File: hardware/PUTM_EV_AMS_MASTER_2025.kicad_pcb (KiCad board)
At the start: 4 copper layers, 60 x 100 mm, 161 parts, among them IC1 3.3V/0.5A, IC11 ISO6760, IC2 TPS54202HDDCR, IC4 ADS131M04, IC5 LTC1799, IC6 LTC6820IMS, IC7 ISO6760, IC8 3.3V/0.5A, J1 M80-5100642, J10 M300-MV10345M1, J12 M80-51034XX, J2 USB_C_Receptacle_USB2.0_14P, J3 M80-51014XX, J4 FTSH-107-01-L-D-K, J5 M80-51004XX, J7 M300-MV10345M1, J8 M80-51004XX, K1 IMB03ITS, U1 MCP2542FD-E/MF, U10 STM32G484VEHx, U12 LMR33640DDDA, U2 LM397, U3 74AUP1G32, U4 UCC12040DVE, U6 MCP2542FD-E/MF, U7 MCP2542FD-E/MF, Y1 X322516MLB4SI

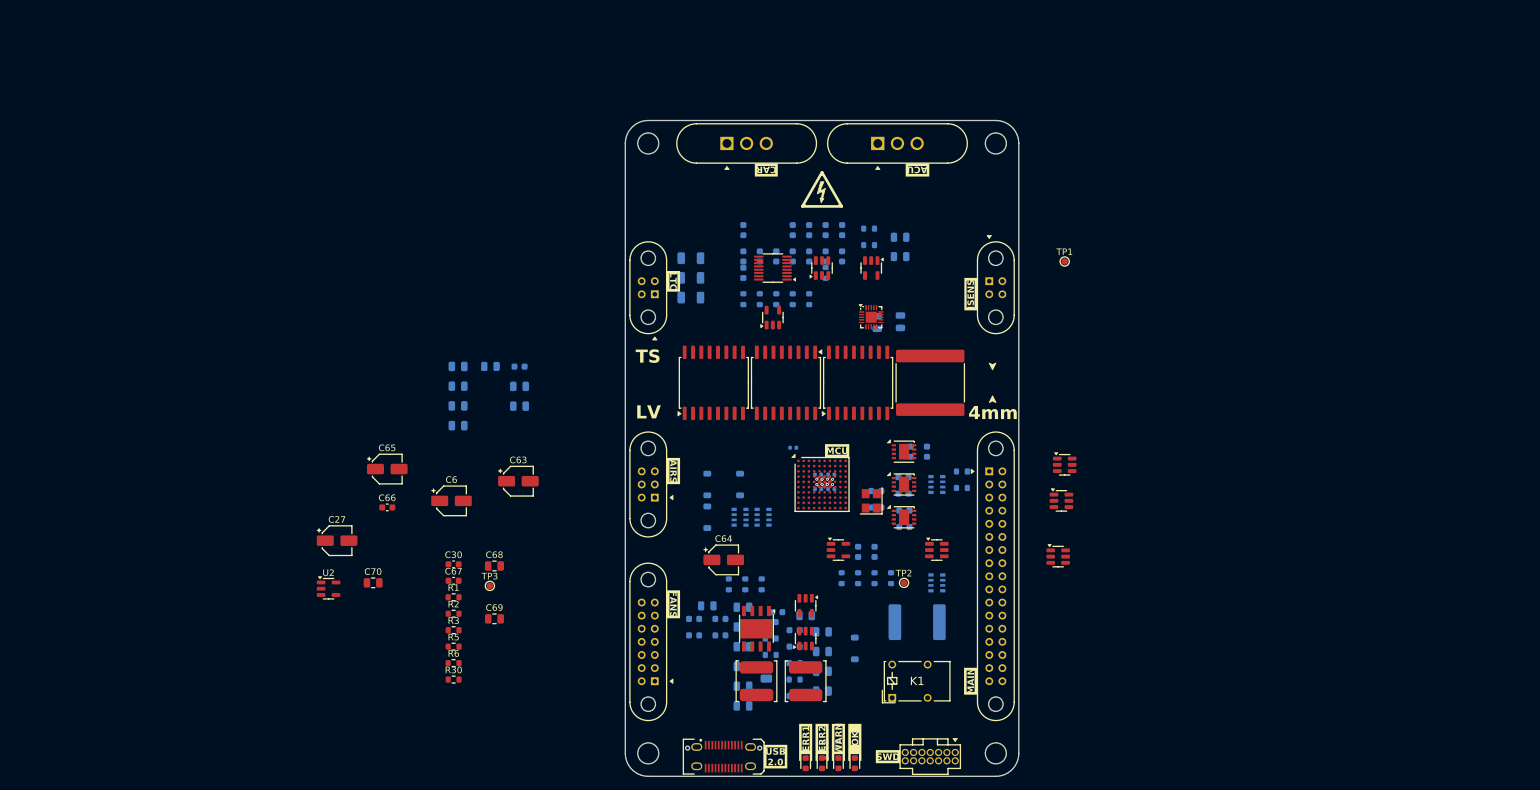
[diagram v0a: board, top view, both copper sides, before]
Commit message: all but the communications sections done
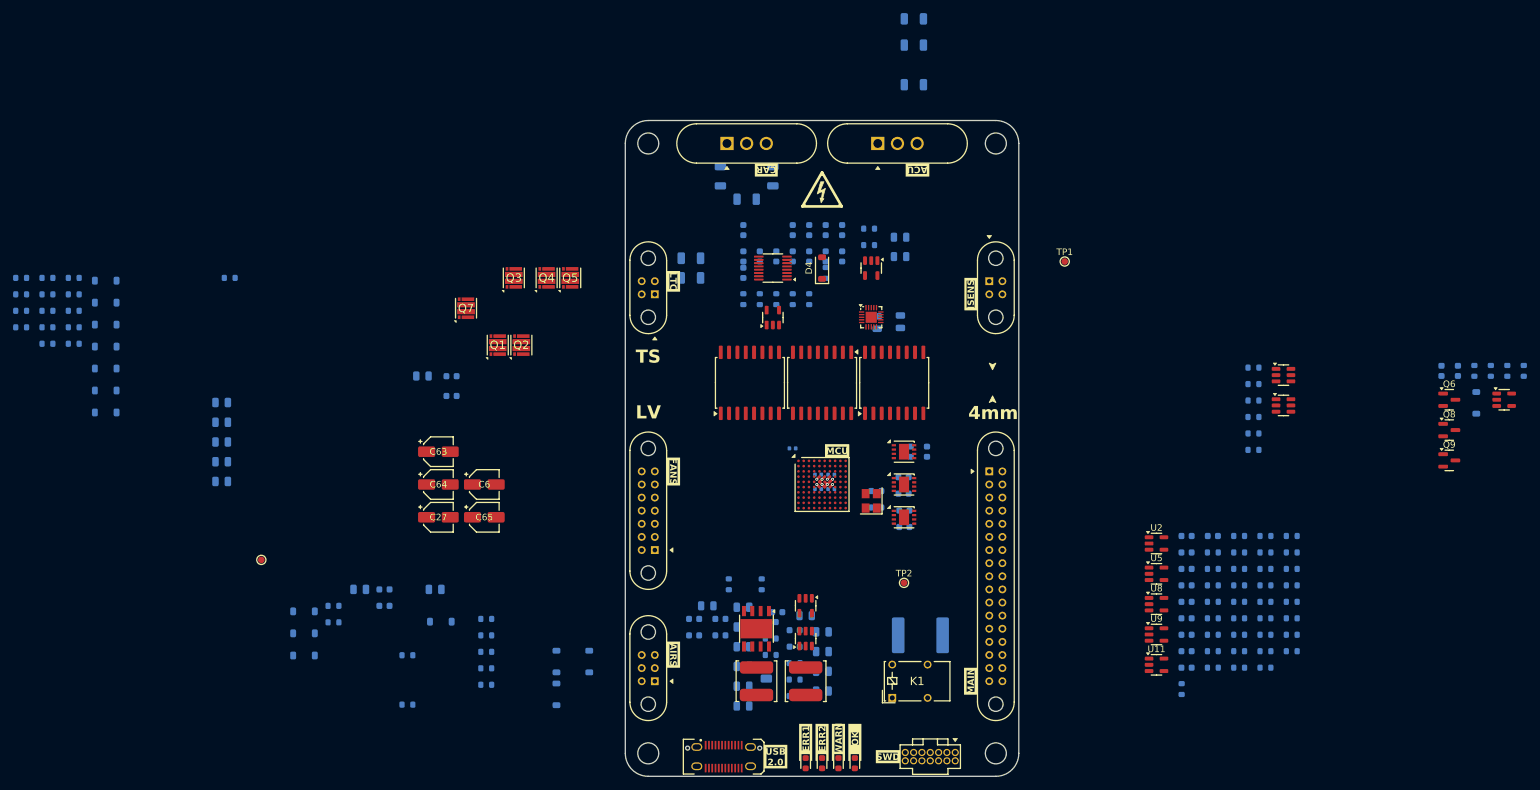
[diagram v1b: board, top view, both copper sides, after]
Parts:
- removed C53: 5.6nF/2000V, Capacitor_SMD:C_3640_9110Metric
- removed D13: ESDA25SC6Y, Package_TO_SOT_SMD:SOT-23-6
- removed RN11: 100, Resistor_SMD:R_Array_Convex_4x0603
- removed RN12: 10k, Resistor_SMD:R_Array_Convex_4x0603
- removed RN16: 1k, Resistor_SMD:R_Array_Convex_4x0603
- removed RN17: 4x100, Resistor_SMD:R_Array_Convex_4x0603
- removed RN7: 4x1k, Resistor_SMD:R_Array_Convex_4x0603
- added C71: 100nF, Capacitor_SMD:C_0603_1608Metric, B.Cu at (300.6, 115.9)
- added C72: 10nF, Capacitor_SMD:C_0603_1608Metric, B.Cu at (300.6, 118.4)
- added C73: 100nF, Capacitor_SMD:C_0603_1608Metric, B.Cu at (300.6, 120.9)
- added C74: 10nF, Capacitor_SMD:C_0603_1608Metric, B.Cu at (300.6, 123.4)
- added C75: 100nF, Capacitor_SMD:C_0603_1608Metric, B.Cu at (300.6, 125.9)
- added C76: 10nF, Capacitor_SMD:C_0603_1608Metric, B.Cu at (300.6, 128.4)
- added C77: 100nF, Capacitor_SMD:C_0603_1608Metric, B.Cu at (304.6, 108.4)
- added D14: 6V, Diode_SMD:D_SOD-123, B.Cu at (166.0, 119.8)
- added D15: 0.5V/1A, Diode_SMD:D_SOD-123, B.Cu at (166.0, 126.6)
- added D16: 30V, Diode_SMD:D_SOD-123, B.Cu at (166.0, 123.2)
- added D17: VSSB410S-E3/52T, Diode_SMD:D_SOD-123, B.Cu at (135.8, 72.8)
- added D18: VSSB410S-E3/52T, Diode_SMD:D_SOD-123, B.Cu at (135.8, 76.1)
- added D19: VSSB410S-E3/52T, Diode_SMD:D_SOD-123, B.Cu at (135.8, 79.5)
- added D20: VSSB410S-E3/52T, Diode_SMD:D_SOD-123, B.Cu at (135.8, 82.8)
- added D21: VSSB410S-E3/52T, Diode_SMD:D_SOD-123, B.Cu at (135.8, 86.2)
- added D22: VSSB410S-E3/52T, Diode_SMD:D_SOD-123, B.Cu at (135.8, 89.5)
- added D8: VSSB410S-E3/52T, Diode_SMD:D_SOD-123, B.Cu at (135.8, 69.4)
- added Q1: DMT6018LDR-7, Samacsys:DMT6018LDR7, F.Cu at (195.6, 79.2)
- added Q2: DMT6018LDR-7, Samacsys:DMT6018LDR7, F.Cu at (199.2, 79.2)
- added Q3: DMT6018LDR-7, Samacsys:DMT6018LDR7, F.Cu at (198.0, 69.0)
- added Q4: DMT6018LDR-7, Samacsys:DMT6018LDR7, F.Cu at (203.0, 69.0)
- added Q5: DMT6018LDR-7, Samacsys:DMT6018LDR7, F.Cu at (206.6, 69.0)
- added Q6: 2N7002, Package_TO_SOT_SMD:SOT-23, F.Cu at (340.6, 87.6)
- added Q7: DMT6018LDR-7, Samacsys:DMT6018LDR7, F.Cu at (190.7, 73.6)
- added Q8: 2N7002, Package_TO_SOT_SMD:SOT-23, F.Cu at (340.6, 92.2)
- added Q9: 2N7002, Package_TO_SOT_SMD:SOT-23, F.Cu at (340.6, 96.8)
- added R15: 10k, Resistor_SMD:R_0603_1608Metric, B.Cu at (304.6, 110.9)
- added R17: 10k, Resistor_SMD:R_0603_1608Metric, B.Cu at (304.6, 113.4)
- added R31: 1k, Resistor_SMD:R_0603_1608Metric, B.Cu at (181.8, 126.5)
- added R32: 10k, Resistor_SMD:R_0603_1608Metric, B.Cu at (304.6, 115.9)
- added R33: TBD, Resistor_SMD:R_0603_1608Metric, B.Cu at (304.6, 118.4)
- added R34: 1k, Resistor_SMD:R_0603_1608Metric, B.Cu at (181.8, 134.1)
- added R35: TBD, Resistor_SMD:R_0603_1608Metric, B.Cu at (304.6, 120.9)
- added R36: 1k, Resistor_SMD:R_0603_1608Metric, B.Cu at (170.5, 119.0)
- added R37: 100, Resistor_SMD:R_0603_1608Metric, B.Cu at (170.5, 121.5)
- added R38: 10k, Resistor_SMD:R_0603_1608Metric, B.Cu at (304.6, 123.4)
- added R39: 10k, Resistor_SMD:R_0603_1608Metric, B.Cu at (304.6, 125.9)
- added R40: 10k, Resistor_SMD:R_0603_1608Metric, B.Cu at (304.6, 128.4)
- added R41: 10k, Resistor_SMD:R_0603_1608Metric, B.Cu at (308.6, 108.4)
- added R42: TBD, Resistor_SMD:R_0603_1608Metric, B.Cu at (308.6, 110.9)
- added R43: TBD, Resistor_SMD:R_0603_1608Metric, B.Cu at (308.6, 113.4)
- added R44: 100, Resistor_SMD:R_0603_1608Metric, B.Cu at (193.8, 121.0)
- added R45: 100, Resistor_SMD:R_0603_1608Metric, B.Cu at (193.8, 123.5)
- added R46: 10k, Resistor_SMD:R_0603_1608Metric, B.Cu at (193.8, 126.0)
- added R47: 10k, Resistor_SMD:R_0603_1608Metric, B.Cu at (193.8, 128.5)
- added R48: 10k, Resistor_SMD:R_0603_1608Metric, B.Cu at (193.8, 131.0)
- added R49: 33, Resistor_SMD:R_0603_1608Metric, B.Cu at (310.8, 87.7)
- added R50: 33, Resistor_SMD:R_0603_1608Metric, B.Cu at (310.8, 90.2)
- added R51: 33, Resistor_SMD:R_0603_1608Metric, B.Cu at (310.8, 92.7)
- added R52: 33, Resistor_SMD:R_0603_1608Metric, B.Cu at (310.8, 95.2)
- added R53: 1M/.1%, Resistor_SMD:R_1206_3216Metric, B.Cu at (229.5, 53.5)
- added R54: 1M/.1%, Resistor_SMD:R_1206_3216Metric, B.Cu at (237.5, 53.5)
- added R55: 100/.1%, Resistor_SMD:R_1206_3216Metric, B.Cu at (233.5, 57.0)
- added R56: 10k, Resistor_SMD:R_0603_1608Metric, B.Cu at (130.9, 74.0)
- added R57: 10k, Resistor_SMD:R_0603_1608Metric, B.Cu at (130.9, 76.5)
- added R58: 100, Resistor_SMD:R_0603_1608Metric, B.Cu at (130.9, 79.0)
- added R59: 100, Resistor_SMD:R_0603_1608Metric, B.Cu at (126.9, 69.0)
- added R60: 10k, Resistor_SMD:R_0603_1608Metric, B.Cu at (126.9, 71.5)
- added R61: 10k, Resistor_SMD:R_0603_1608Metric, B.Cu at (126.9, 74.0)
- added R62: 100, Resistor_SMD:R_0603_1608Metric, B.Cu at (126.9, 76.5)
- added R63: 100, Resistor_SMD:R_0603_1608Metric, B.Cu at (126.9, 79.0)
- added R64: 10k, Resistor_SMD:R_0603_1608Metric, B.Cu at (122.9, 69.0)
- added R65: 10k, Resistor_SMD:R_0603_1608Metric, B.Cu at (122.9, 71.5)
- added R66: 100, Resistor_SMD:R_0603_1608Metric, B.Cu at (122.9, 74.0)
- added R67: 10k, Resistor_SMD:R_0603_1608Metric, B.Cu at (122.9, 76.5)
- added R68: TBD, Resistor_SMD:R_0603_1608Metric, B.Cu at (308.6, 115.9)
- added R69: TBD, Resistor_SMD:R_0603_1608Metric, B.Cu at (308.6, 118.4)
- added R70: 10k, Resistor_SMD:R_0603_1608Metric, B.Cu at (308.6, 120.9)
- added R71: 10k, Resistor_SMD:R_0603_1608Metric, B.Cu at (308.6, 123.4)
- added R72: 10k, Resistor_SMD:R_0603_1608Metric, B.Cu at (308.6, 125.9)
- added R73: 10k, Resistor_SMD:R_0603_1608Metric, B.Cu at (308.6, 128.4)
- added R74: TBD, Resistor_SMD:R_0603_1608Metric, B.Cu at (312.6, 108.4)
- added R75: TBD, Resistor_SMD:R_0603_1608Metric, B.Cu at (312.6, 110.9)
- added R76: TBD, Resistor_SMD:R_0603_1608Metric, B.Cu at (312.6, 113.4)
- added R77: 10k, Resistor_SMD:R_0603_1608Metric, B.Cu at (312.6, 115.9)
- added R78: 10k, Resistor_SMD:R_0603_1608Metric, B.Cu at (312.6, 118.4)
- added R79: 10k, Resistor_SMD:R_0603_1608Metric, B.Cu at (312.6, 120.9)
- added R80: 10k, Resistor_SMD:R_0603_1608Metric, B.Cu at (312.6, 123.4)
- added R81: TBD, Resistor_SMD:R_0603_1608Metric, B.Cu at (312.6, 125.9)
- added R82: TBD, Resistor_SMD:R_0603_1608Metric, B.Cu at (312.6, 128.4)
- added R83: TBD, Resistor_SMD:R_0603_1608Metric, B.Cu at (316.6, 108.4)
- added R84: 10k, Resistor_SMD:R_0603_1608Metric, B.Cu at (316.6, 110.9)
- added R85: 10k, Resistor_SMD:R_0603_1608Metric, B.Cu at (316.6, 113.4)
- added R86: 10k, Resistor_SMD:R_0603_1608Metric, B.Cu at (316.6, 115.9)
- added R87: 10k, Resistor_SMD:R_0603_1608Metric, B.Cu at (316.6, 118.4)
- added R88: TBD, Resistor_SMD:R_0603_1608Metric, B.Cu at (316.6, 120.9)
- added R89: TBD, Resistor_SMD:R_0603_1608Metric, B.Cu at (316.6, 123.4)
- added R90: TBD, Resistor_SMD:R_0603_1608Metric, B.Cu at (316.6, 125.9)
- added U11: LM397, Package_TO_SOT_SMD:SOT-23-5, F.Cu at (296.0, 128.0)
- added U5: LM397, Package_TO_SOT_SMD:SOT-23-5, F.Cu at (296.0, 114.1)
- added U8: LM397, Package_TO_SOT_SMD:SOT-23-5, F.Cu at (296.0, 118.8)
- added U9: LM397, Package_TO_SOT_SMD:SOT-23-5, F.Cu at (296.0, 123.4)
- C30, C66, C67, C68, C69, C70: moved to B.Cu
- C4: value 100nF -> 220nF; footprint Capacitor_SMD:C_0805_2012Metric -> Capacitor_SMD:C_0603_1608Metric
- C5: value 100nF -> 10nF; footprint Capacitor_SMD:C_0805_2012Metric -> Capacitor_SMD:C_0603_1608Metric
- C50: value 10nF/1kV -> 100nF; footprint Capacitor_SMD:C_1206_3216Metric -> Capacitor_SMD:C_0603_1608Metric
- D4: value ESDA5V3SC5 -> 0.5/5A; footprint Package_TO_SOT_SMD:SOT-23-6 -> Diode_SMD:D_SOD-123
- D5: value ESDA5V3SC5 -> 0.1/1A; footprint Package_TO_SOT_SMD:SOT-23-6 -> Diode_SMD:D_SOD-123; moved to B.Cu
- IC1: value 3.3V/0.5A -> TPS7B92033DBVR
- L2: value 6.8uF -> 6.8uF/3.5A
- R1, R2: value 10M -> 1M/.1%; footprint Resistor_SMD:R_0603_1608Metric -> Resistor_SMD:R_1206_3216Metric; moved to B.Cu
- R27: value 10k -> 1k
- R3: value 10M -> 0; moved to B.Cu
- R30: value 1k -> 100; moved to B.Cu
- R4: value 10k -> TBD
- R5: value 10M -> 100; moved to B.Cu
- R6: value 1k -> 100/.1%; footprint Resistor_SMD:R_0603_1608Metric -> Resistor_SMD:R_1206_3216Metric; moved to B.Cu
- moved U2 126.4 mm to (296.0, 109.5)
- moved C66 122.2 mm to (300.6, 113.4), turned to 180 degrees
- moved R1 112.7 mm to (259.0, 29.5), turned to 180 degrees
- moved R6 112.7 mm to (259.0, 39.5), turned to 180 degrees
- moved R2 111.6 mm to (259.0, 33.5), turned to 180 degrees
- moved U3 104.1 mm to (349.0, 87.6)
- moved C5 103.6 mm to (300.6, 108.4)
- moved D7 101.9 mm to (344.8, 88.1)
- moved R11 101.5 mm to (344.5, 83.2)
- moved R12 101.5 mm to (347.0, 83.2)
- moved R13 101.5 mm to (349.5, 83.2)
- moved R14 101.5 mm to (352.0, 83.2)
- moved D5 94.7 mm to (186.9, 121.4), turned to 180 degrees
- moved C7 93.1 mm to (339.4, 83.2)
- moved C8 93.1 mm to (342.0, 83.2)
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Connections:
- net /IMD_SENSENSOR renamed /IMD_SENSOR
- C23 pad 1: +3.3V -> +3.3VIO
- C24 pad 1: +3.3V -> +3.3VIO
- C25 pad 1: +3.3V -> +3.3VIO
- C28 pad 1: +3.3V -> +3.3VIO
- C29 pad 1: +3.3V -> +3.3VIO
- C4 pad 1: GND -> +24V
- C4 pad 2: +24V -> GND
- C5 pad 1: GND -> Net-(C5-Pad1)
- C5 pad 2: +24V -> GND
- C50 pad 1: /ISO_SPI_SH -> Net-(C50-Pad1)
- C50 pad 2: GNDISO -> GND
- C66 pad 1: Net-(C66-Pad1) -> +24V
- C66 pad 2: unconnected-(C66-Pad2) -> GND
- C70 pad 1: +3.3V -> +3.3VIO
- D12 pad 1: Net-(RN17-R4.2) -> /Connectivity/UC_SPI_CS
- D12 pad 3: Net-(RN17-R3.2) -> /Connectivity/UC_SPI_SCK
- D12 pad 4: Net-(RN17-R2.2) -> /Connectivity/UC_SPI_MISO
- D12 pad 6: Net-(RN17-R1.2) -> /Connectivity/UC_SPI_MOSI
- D4 pad 1: Net-(RN13D-R4.1) -> +24V
- D4 pad 2: GNDISO -> Net-(D16-K)
- D5 pad 1: /Connectivity/EX_IN3 -> Net-(D14-K)
- D5 pad 2: GND -> VBUS+
- D7 pad 1: +24V -> +5V
- J5 pad 3: /ISO_SPI_SH -> Net-(J5-Pin_3)
- J5 pad 4: /ISO_SPI_SH -> Net-(J5-Pin_3)
- K1 pad 8: +24V -> +5V
- R26 pad 1: /Connectivity/UC_IN2 -> +3.3V
- R26 pad 2: /Connectivity/EX_IN2 -> Net-(R17-Pad1)
- R27 pad 1: /Connectivity/UC_IN3 -> /SIGNAL_LED_1
- R27 pad 2: /Connectivity/EX_IN3 -> /LED1
- R3 pad 1: /Isolated ADC/CAR+ -> +3.3V
- R3 pad 2: /Isolated ADC/CAR_V+ -> +3.3VIO
- R30 pad 1: /Isolated ADC/CAR- -> /Fan Control/FAN2_CTRL
- R30 pad 2: /Isolated ADC/CAR+ -> Net-(Q2B-G2)
- R4 pad 1: /Connectivity/UC_IN1 -> /Isolated ADC/I-
- R4 pad 2: /Connectivity/EX_IN1 -> GNDISO
- R5 pad 1: /Isolated ADC/CAR_V- -> /Fan Control/FAN1_CTRL
- R5 pad 2: /Isolated ADC/CAR- -> Net-(Q2A-G1)
- U10 pad D5: +3.3V -> +3.3VIO
- U10 pad D7: +3.3V -> +3.3VIO
- U10 pad F5: +3.3V -> +3.3VIO
- U10 pad F7: +3.3V -> +3.3VIO
- U10 pad J5: +3.3V -> +3.3VIO
- U10 pad K5: +3.3V -> +3.3VIO
- U2 pad 1: unconnected-(U2-Pad1) -> Net-(R17-Pad1)
- U2 pad 2: unconnected-(U2-Pad2) -> GND
- U2 pad 3: unconnected-(U2-Pad3) -> Net-(C5-Pad1)
- U2 pad 4: unconnected-(U2-Pad4) -> /Connectivity/UC_IN2
- U2 pad 5: Net-(C66-Pad1) -> +24V
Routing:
- net +3.3VIO: track 0.00 -> 2.26 mm, vias 0 -> 4
- net +3.3V: track 2.26 -> 0.00 mm, vias 4 -> 0

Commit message: sync
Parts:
- added C53: 100nF, Capacitor_SMD:C_0603_1608Metric, F.Cu at (89.1, 58.5)
- added C78: 100nF, Capacitor_SMD:C_0603_1608Metric, F.Cu at (70.2, 49.9)
- added C79: 100p, Capacitor_SMD:C_0603_1608Metric, F.Cu at (70.2, 52.4)
- added C80: 100p, Capacitor_SMD:C_0603_1608Metric, F.Cu at (70.2, 55.0)
- added IC3: BQ79600PWRQ1, Package_SO:TSSOP-16_4.4x5mm_P0.65mm, F.Cu at (136.0, 75.0)
- added R91: 5.1k, Resistor_SMD:R_0603_1608Metric, F.Cu at (95.1, 64.2)
- added R92: 5.1k, Resistor_SMD:R_0603_1608Metric, F.Cu at (95.1, 66.7)
- added R93: 10k, Resistor_SMD:R_0603_1608Metric, F.Cu at (85.2, 67.5)
- added R94: 10k, Resistor_SMD:R_0603_1608Metric, F.Cu at (79.2, 67.5)
- added R95: 100k, Resistor_SMD:R_0603_1608Metric, F.Cu at (70.2, 57.5)
- added R96: 51, Resistor_SMD:R_0603_1608Metric, F.Cu at (70.2, 60.0)
- added R97: 1k, Resistor_SMD:R_0603_1608Metric, F.Cu at (70.2, 62.5)
- added R98: 51, Resistor_SMD:R_0603_1608Metric, F.Cu at (70.2, 65.0)
- added R99: 100k, Resistor_SMD:R_0603_1608Metric, F.Cu at (70.2, 67.5)
- added T1: >100kHz, Samacsys:SOP254P914X350-4N, F.Cu at (120.5, 78.0)
- C36: value 10nF/1kV -> 22uF; footprint Capacitor_SMD:C_1206_3216Metric -> Capacitor_SMD:C_0805_2012Metric
- C43: value 10nF/1kV -> 220nF; footprint Capacitor_SMD:C_1206_3216Metric -> Capacitor_SMD:C_0603_1608Metric; moved to F.Cu
- D4: moved to B.Cu
- R4: value TBD -> 10k
- moved C43 144.1 mm to (81.1, 62.0), turned to 0 degrees
- moved Q2 114.0 mm to (85.2, 81.3)
- moved Q1 109.4 mm to (86.5, 87.5)
- moved R11 109.3 mm to (235.5, 90.7)
- moved R12 109.3 mm to (238.0, 90.7)
- moved R41 109.3 mm to (199.6, 115.9)
- moved R42 109.3 mm to (199.6, 118.4)
- moved R43 109.3 mm to (199.6, 120.9)
- moved R49 109.3 mm to (201.8, 95.2)
- moved R50 109.3 mm to (201.8, 97.7)
- moved R51 109.3 mm to (201.8, 100.2)
- moved R52 109.3 mm to (201.8, 102.7)
- moved R68 109.3 mm to (199.6, 123.4)
- moved R69 109.3 mm to (199.6, 125.9)
- moved R7 109.3 mm to (201.8, 90.2)
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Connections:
- net /ISO_LTC_MISO renamed /ISO_COM_MISO
- net /ISO_LTC_MOSI renamed /ISO_COM_MOSI
- net /ISO_LTC_SCK renamed /ISO_COM_SCK
- net /MCU/LTC_MISO renamed /MCU/COM_MISO
- net /MCU/LTC_MOSI renamed /MCU/COM_MOSI
- net /MCU/LTC_SCK renamed /MCU/COM_SCK
- net /MCU/~{LTC_CS} renamed /MCU/~{COM_CS}
- net /~{ISO_LTC_CS} renamed /~{ISO_COM_CS}
- C36 pad 1: Net-(J5-Pin_1) -> +3.3VIO
- C36 pad 2: /Isolated SPI/OUT- -> GND
- C43 pad 1: Net-(J5-Pin_2) -> GNDISO
- C43 pad 2: /Isolated SPI/OUT+ -> +5VISO
- F7 pad 1: I_VDDISO -> +5VISO
- J12 pad 30: /IMD_SENSOR -> unconnected-(J12-Pin_30-Pad30)
- J2 pad A5: unconnected-(J2-CC1-PadA5) -> Net-(J2-CC1)
- J2 pad B5: unconnected-(J2-CC2-PadB5) -> Net-(J2-CC2)
- J5 pad 3: Net-(J5-Pin_3) -> unconnected-(J5-Pin_3-Pad3)
- J5 pad 4: Net-(J5-Pin_3) -> unconnected-(J5-Pin_4-Pad4)
- J8 pad 3: I_VDDISO -> +5VISO
- R33 pad 2: /Connectivity/EX_IN2 -> /CHARGER_DETECTION
- R42 pad 2: /Connectivity/EX_IN1 -> TSMS
- R49 pad 2: /Connectivity/EX_SPI_SCK -> /EXT_SCK
- R50 pad 2: /Connectivity/EX_SPI_CS -> /~{EXT_CS}
- R51 pad 2: /Connectivity/EX_SPI_MISO -> /EXT_MISO
- R52 pad 2: /Connectivity/EX_SPI_MOSI -> /EXT_MOSI
- R7 pad 2: /Connectivity/EX_D+ -> /D+
- R70 pad 2: /Connectivity/UC_AIR_AUX_PRE -> /AIR_PRE_DETECTION
- R71 pad 2: /Connectivity/UC_AIR_AUX_PRE -> /AIR_PRE_DETECTION
- R8 pad 2: /Connectivity/EX_D- -> /D-
- R83 pad 2: /Connectivity/EX_AIR_AUX_M -> /AIR_M_DETECTION
- R90 pad 2: /Connectivity/EX_AIR_AUX_P -> /AIR_P_DETECTION
- U1 pad 6: /Connectivity/EX_CANFD3- -> /CANFD3-
- U1 pad 7: /Connectivity/EX_CANFD3+ -> /CANFD3+
- U10 pad A4: /MCU/CANFD2_TX -> /Connectivity/UC_CANFD2_TX
- U10 pad A5: /MCU/CANFD3_RX -> /Connectivity/UC_CANFD3_RX
- U10 pad A6: /MCU/DETECT_AIR_P -> /Connectivity/UC_AIR_AUX_P
- U10 pad A7: /MCU/DETECT_AIR_PRE -> /Connectivity/EX_AIR_AUX_PRE
- U10 pad A8: /MCU/DETECT_AIR_M -> /Connectivity/UC_AIR_AUX_M
- U10 pad A9: /MCU/CANFD1_TX -> /Connectivity/UC_CANFD1_TX
- U10 pad B5: /MCU/CANFD2_RX -> /Connectivity/UC_CANFD2_RX
- U10 pad B6: /MCU/DETECT_CHARGER -> /Connectivity/UC_IN2
- U10 pad B7: /MCU/DETECT_TSMS -> /Connectivity/UC_IN1
- U10 pad B8: /MCU/CANFD1_RX -> /Connectivity/UC_CANFD1_RX
- U10 pad C10: /MCU/D- -> /Connectivity/UC_D-
- U10 pad C5: /MCU/CANFD3_TX -> /Connectivity/UC_CANFD3_TX
- U10 pad C9: /MCU/D+ -> /Connectivity/UC_D+
- U10 pad F2: unconnected-(U10-PC0-PadF2) -> /MCU/EN_12V
- U10 pad F4: unconnected-(U10-PC1-PadF4) -> /MCU/PG_12V
- U10 pad H2: /MCU/~{EXT_CS} -> /Connectivity/UC_SPI_CS
- U10 pad J1: /MCU/EXT_SCK -> /Connectivity/UC_SPI_SCK
- U10 pad J2: /MCU/EXT_MISO -> /Connectivity/UC_SPI_MISO
- U10 pad J4: /MCU/SENS_IMD -> unconnected-(U10-PB2-PadJ4)
- U10 pad K1: /MCU/EXT_MOSI -> /Connectivity/UC_SPI_MOSI
- U6 pad 6: /Connectivity/EX_CANFD2- -> /CANFD2-
- U6 pad 7: /Connectivity/EX_CANFD2+ -> /CANFD2+
- U7 pad 6: /Connectivity/EX_CANFD1- -> /CANFD1-
- U7 pad 7: /Connectivity/EX_CANFD1+ -> /CANFD1+
- U8 pad 4: /Connectivity/UC_AIR_AUX_PRE -> /AIR_PRE_DETECTION

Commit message: sync
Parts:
- moved C4 176.8 mm to (255.7, 108.8)
- moved D14 174.8 mm to (228.8, 95.3)
- moved C68 172.2 mm to (244.9, 85.7)
- moved F8 158.9 mm to (233.9, 91.8)
- moved TP3 156.8 mm to (201.3, 76.7)
- moved D5 155.4 mm to (228.8, 92.0)
- moved C3 154.3 mm to (233.7, 94.5)
- moved D16 151.6 mm to (200.2, 80.8)
- moved C6 145.5 mm to (229.8, 99.9)
- moved F3 141.4 mm to (266.0, 110.3)
- moved L2 136.7 mm to (261.5, 119.9)
- moved L4 136.4 mm to (254.9, 76.0)
- moved U12 136.2 mm to (261.0, 111.8)
- moved C21 130.4 mm to (249.1, 73.4)
- moved C22 130.4 mm to (249.1, 75.9)
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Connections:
- net Net-(C5-Pad1) renamed /Connectivity/EI2
- net Net-(C50-Pad1) renamed /Connectivity/EI1
- net Net-(C72-Pad1) renamed /Connectivity/EAAE
- net Net-(C74-Pad1) renamed /Connectivity/EAAM
- net Net-(C76-Pad1) renamed /Connectivity/EAAP
- net Net-(J5-Pin_1) renamed /CCO+
- net Net-(J5-Pin_2) renamed /CCO-
- IC11 pad 11: unconnected-(IC11-OUTE-Pad11) -> /MCU/~{FLT}
- IC11 pad 12: unconnected-(IC11-OUTD-Pad12) -> /MCU/SPI_RDY
- IC11 pad 5: GNDISO -> /SPI_RDY
- IC11 pad 6: GNDISO -> /~{FLT}
- IC3 pad 2: /Isolated SPI/~{FLT} -> /~{FLT}
- IC3 pad 8: /Isolated SPI/SPI_RDY -> /SPI_RDY
- IC6 pad 10: /Isolated SPI/OUT- -> /OUT-
- IC6 pad 11: /Isolated SPI/OUT+ -> /OUT+
- R20 pad 1: /Isolated SPI/OUT+ -> /OUT+
- R20 pad 2: /Isolated SPI/OUT- -> /OUT-
- R95 pad 2: /Isolated SPI/SPI_RDY -> /SPI_RDY
- R96 pad 1: /Isolated SPI/OUT+ -> /OUT+
- R98 pad 1: /Isolated SPI/OUT- -> /OUT-
- R99 pad 2: /Isolated SPI/~{FLT} -> /~{FLT}
- T1 pad 3: /Isolated SPI/OUT- -> /OUT+
- T1 pad 4: /Isolated SPI/OUT+ -> /OUT-
- U10 pad F1: unconnected-(U10-PC2-PadF1) -> /MCU/SPI_RDY
- U10 pad G1: unconnected-(U10-PC3-PadG1) -> /MCU/~{FLT}
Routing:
- net +24V: track 0.00 -> 12.7 mm, vias 0 -> 5
- net GND: track 4.53 -> 17.1 mm, vias 4 -> 10
- net Net-(R71-Pad1): track 0.00 -> 7.43 mm, vias 0 -> 1
- net Net-(R78-Pad1): track 0.00 -> 7.43 mm, vias 0 -> 1
- net Net-(R39-Pad1): track 0.00 -> 7.43 mm, vias 0 -> 1
- net Net-(R85-Pad1): track 0.00 -> 7.43 mm, vias 0 -> 1
- net Net-(R17-Pad1): track 0.00 -> 7.43 mm, vias 0 -> 1
- net /Connectivity/EI1: track 0.00 -> 6.79 mm, vias 0 -> 1
- net /Connectivity/EAAM: track 0.00 -> 6.79 mm, vias 0 -> 1
- net /Connectivity/EAAE: track 0.00 -> 6.79 mm, vias 0 -> 1
- net /Connectivity/EI2: track 0.00 -> 6.79 mm, vias 0 -> 1
- net /Connectivity/EAAP: track 0.00 -> 6.79 mm, vias 0 -> 1
- net +5V: track 0.00 -> 6.41 mm, vias 0 -> 3
- net +3.3V: track 0.00 -> 6.10 mm, vias 0 -> 3
- net +3.3VIO: track 2.26 -> 7.48 mm, vias 4 -> 5
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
